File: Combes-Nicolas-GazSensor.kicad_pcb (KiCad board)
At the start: 2 copper layers, 68.6 x 53.3 mm, 20 parts, among them P1 Power, P2 Analog, P3 Digital, P4 Digital, P5 CONN_01X01, P6 CONN_01X01, P7 CONN_01X01, P8 CONN_01X01

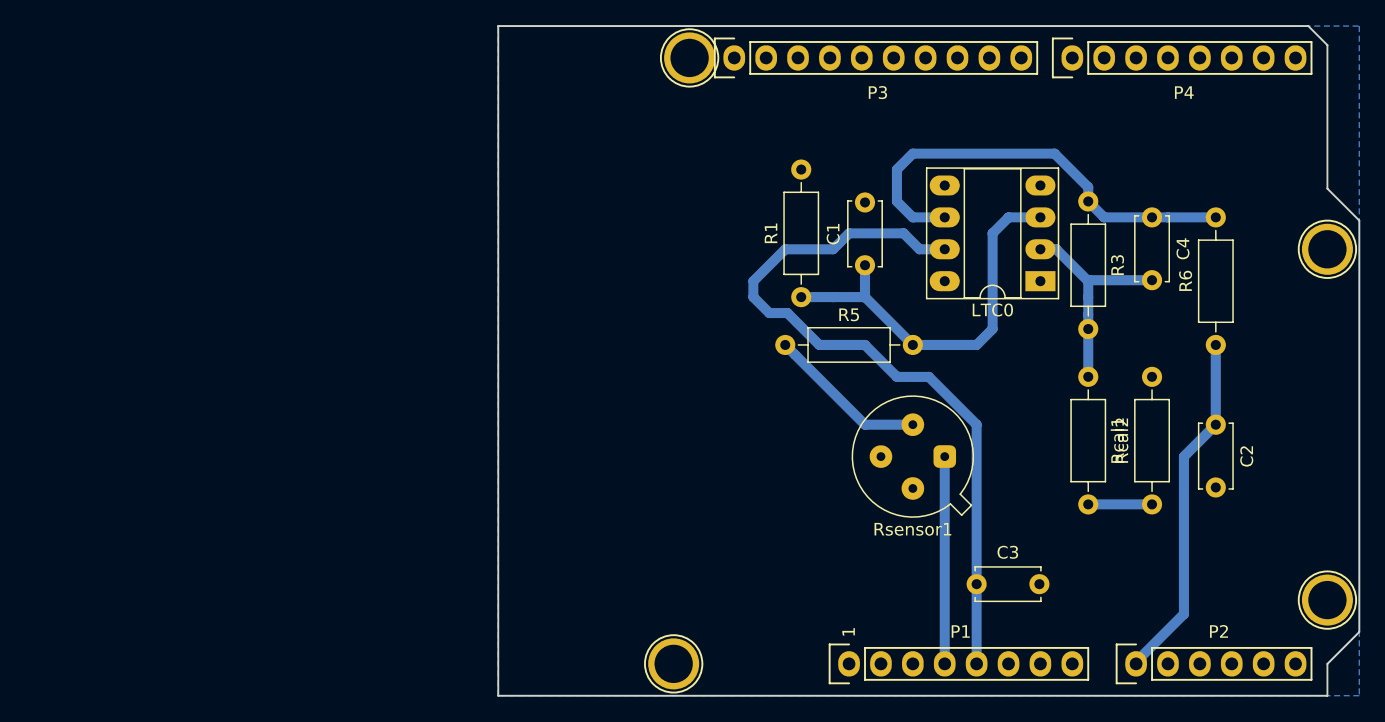
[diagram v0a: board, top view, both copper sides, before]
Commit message: Version avec RN2483 Breakout et routage
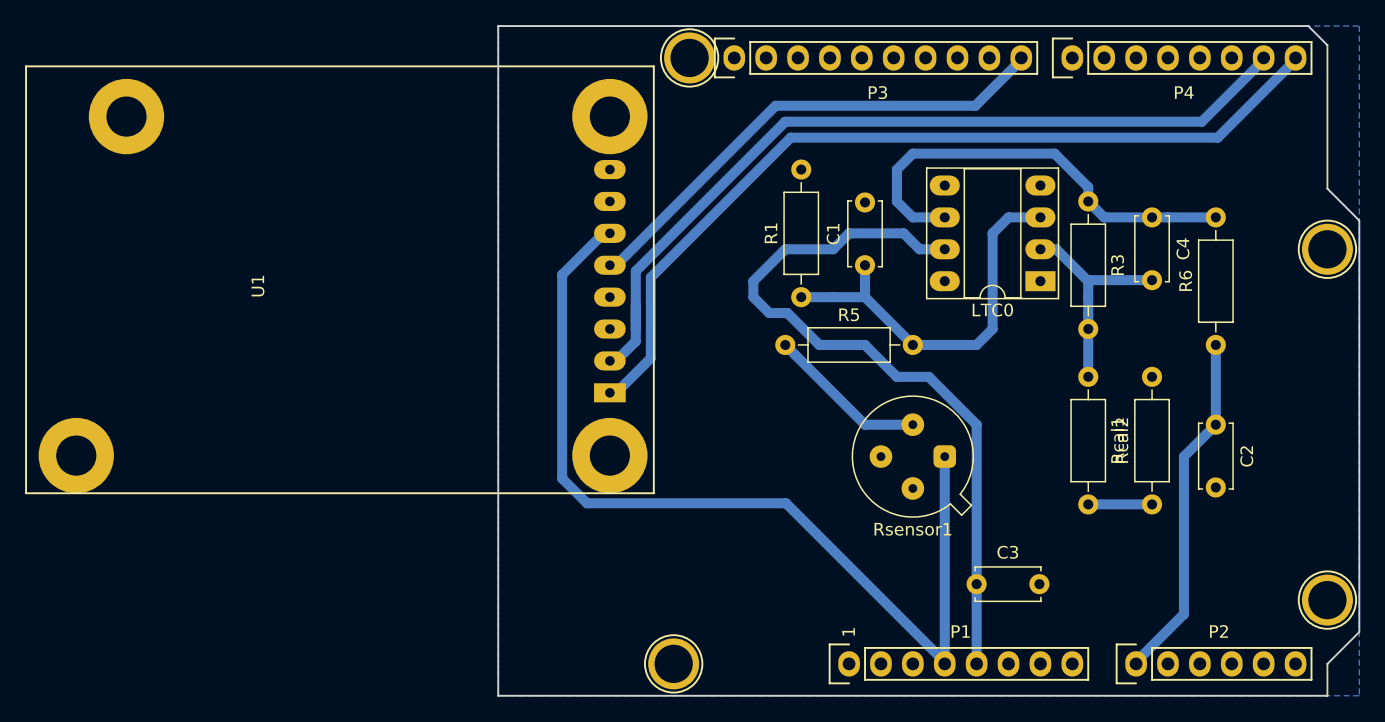
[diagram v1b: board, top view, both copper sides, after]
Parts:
- added U1: RN2483_Breakout, MesEmpreintes:RN2483_Breakout, F.Cu at (119.9, 102.2)
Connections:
- LTC0 pad 1: (no net) -> Net-(LTC0-Pad1)
- LTC0 pad 5: (no net) -> Net-(LTC0-Pad5)
- LTC0 pad 8: (no net) -> Net-(LTC0-Pad8)
- P1 pad 1: (no net) -> Net-(P1-Pad1)
- P1 pad 2: (no net) -> /IOREF
- P1 pad 3: (no net) -> /Reset
- P1 pad 8: (no net) -> /Vin
- P2 pad 2: (no net) -> /A1
- P2 pad 3: (no net) -> /A2
- P2 pad 4: (no net) -> /A3
- P2 pad 5: (no net) -> Net-(P2-Pad5)
- P2 pad 6: (no net) -> Net-(P2-Pad6)
- P3 pad 1: (no net) -> /A5(SCL)
- P3 pad 10: (no net) -> D8
- P3 pad 2: (no net) -> /A4(SDA)
- P3 pad 3: (no net) -> /AREF
- P3 pad 5: (no net) -> /13(SCK)
- P3 pad 6: (no net) -> /12(MISO)
- P3 pad 7: (no net) -> /11(**/MOSI)
- P3 pad 8: (no net) -> /10(**/SS)
- P3 pad 9: (no net) -> /9(**)
- P4 pad 1: (no net) -> /7
- P4 pad 2: (no net) -> /6(**)
- P4 pad 3: (no net) -> /5(**)
- P4 pad 4: (no net) -> /4
- P4 pad 5: (no net) -> /3(**)
- P4 pad 6: (no net) -> /2
- P4 pad 7: (no net) -> Tx
- P4 pad 8: (no net) -> Rx
- P5 pad 1: (no net) -> Net-(P5-Pad1)
- P6 pad 1: (no net) -> Net-(P6-Pad1)
- P7 pad 1: (no net) -> Net-(P7-Pad1)
- P8 pad 1: (no net) -> Net-(P8-Pad1)
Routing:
- net Rx: track 0.00 -> 69.5 mm
- net Tx: track 0.00 -> 67.3 mm
- net +3V3: track 16.5 -> 74.6 mm
- net D8: track 0.00 -> 39.7 mm
